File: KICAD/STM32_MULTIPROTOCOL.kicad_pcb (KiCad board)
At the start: 2 copper layers, 80 x 80 mm, 78 parts, among them T1 TestPoint, T10 TestPoint, T11 TestPoint, T12 TestPoint, T13 TestPoint, T14 TestPoint, T2 TestPoint, T3 TestPoint, T4 TestPoint, T5 TestPoint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

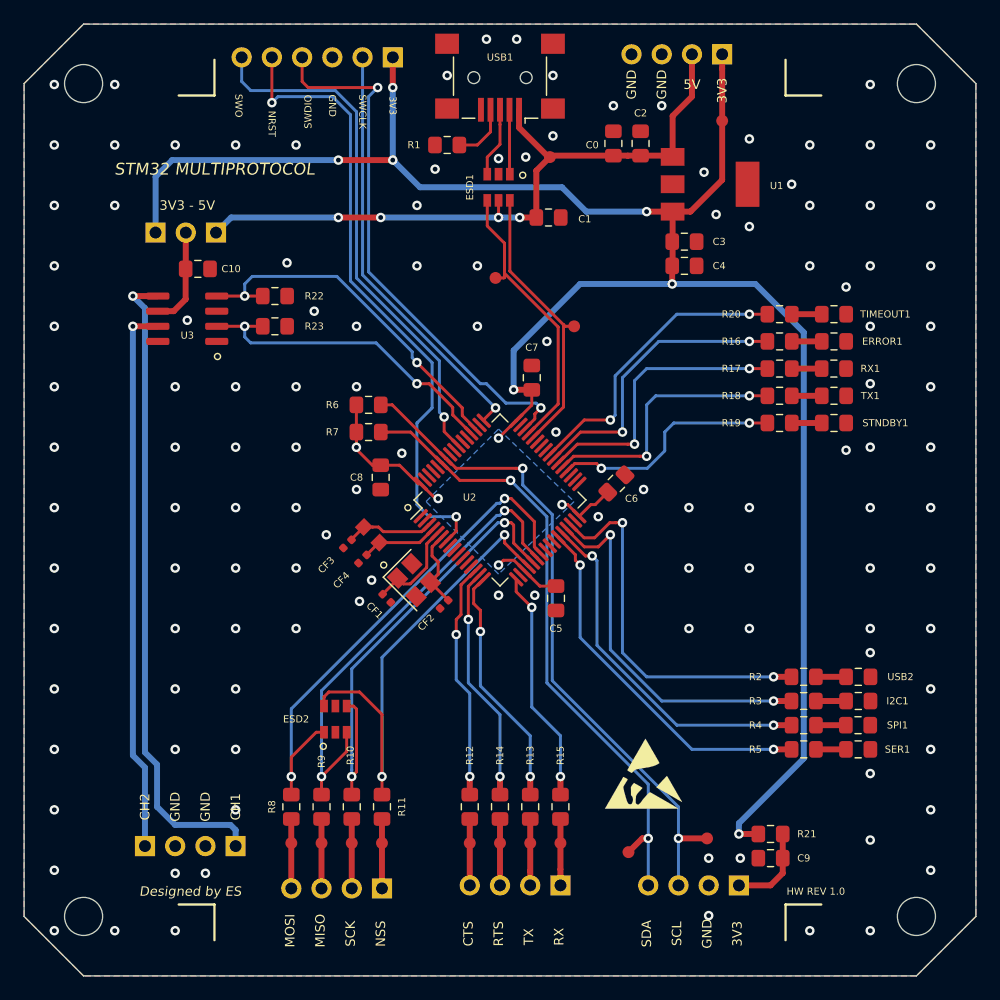
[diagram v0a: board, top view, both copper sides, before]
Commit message: uart,spi,iic pins init in input mode. USB enable fixed.
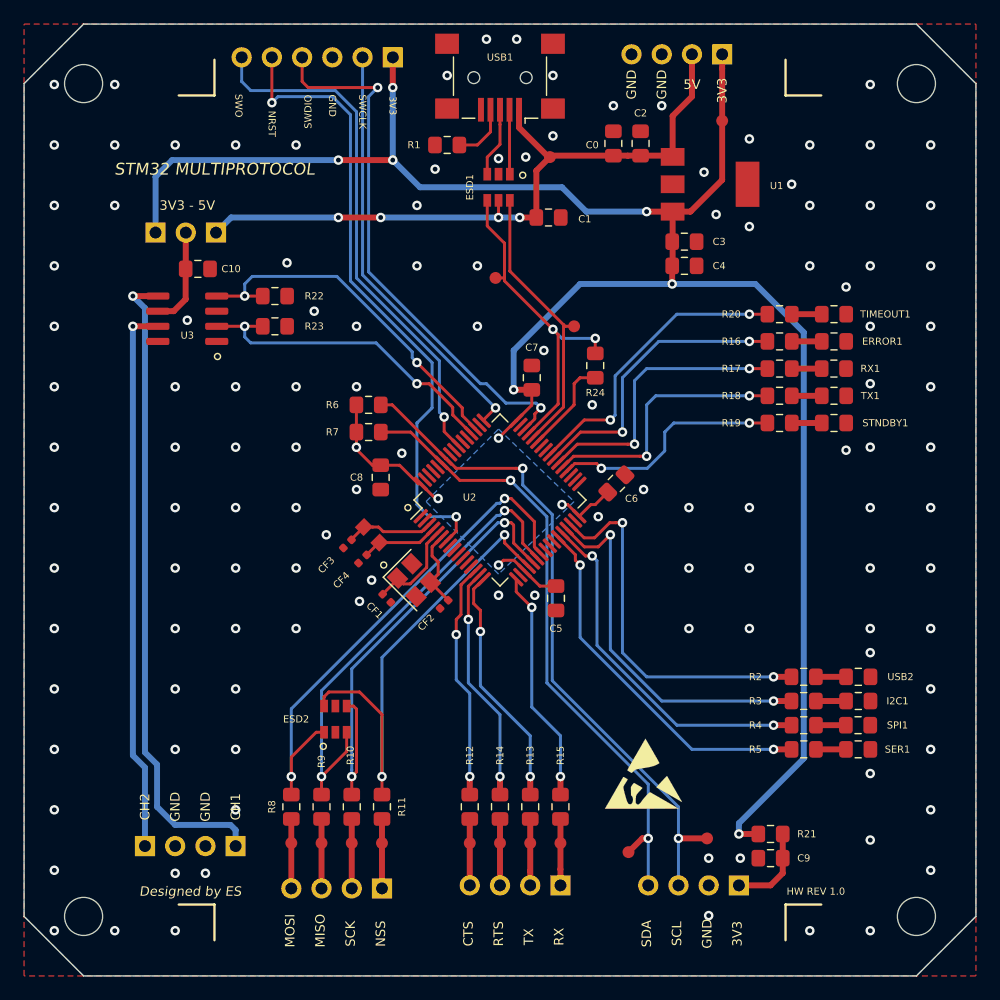
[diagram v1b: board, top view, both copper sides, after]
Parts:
- added R24: 1.5k, Resistor_SMD:R_0805_2012Metric_Pad1.15x1.40mm_HandSolder, F.Cu at (168.0, 88.7)
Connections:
- U2 pad 13: Net-(U2-Pad13) -> +3V3
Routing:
- net Net-(R24-Pad1): track 0.00 -> 8.15 mm
- net USB_DATA+: track 24.2 -> 29.0 mm, vias 0 -> 2

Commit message: added detailed BOM of the boards
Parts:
- U1: value MCP1703A-1202_SOT223 -> MIC39100-3.3WS
- renumbered Y2 to Y1, 48Mhz1 to Y2

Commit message: added pcb revision 2, fixed firmware project for cloners
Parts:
- added C11: 100nF, Resistor_SMD:R_0805_2012Metric_Pad1.15x1.40mm_HandSolder, F.Cu at (172.3, 108.8)
- added MCO1: TestPoint, TestPoint:TestPoint_Pad_D1.0mm, F.Cu at (171.3, 91.5)
- added R25: 10k, Resistor_SMD:R_0805_2012Metric_Pad1.15x1.40mm_HandSolder, F.Cu at (178.9, 99.1)
- added R26: 10k, Resistor_SMD:R_0805_2012Metric_Pad1.15x1.40mm_HandSolder, F.Cu at (178.9, 101.4)
- added TP15: TestPoint, TestPoint:TestPoint_Pad_D1.5mm, F.Cu at (177.9, 124.0)
- added U4: M24C02-WMN, Package_SO:SOIC-8_3.9x4.9mm_P1.27mm, F.Cu at (177.4, 105.7)
- T10, T11, T12, T13, T14, T5, T6, T7, T8, T9: footprint TestPoint:TestPoint_Pad_D1.0mm -> TestPoint:TestPoint_Pad_D1.5mm
- moved C9 4.78 mm to (181.2, 125.6), turned to 180 degrees
- moved R21 2.77 mm to (180.1, 128.8), turned to 90 degrees
- moved C6 2.29 mm to (169.8, 100.9), turned to 0 degrees
- moved T11 0.28 mm to (162.5, 129.6)
- moved T7 0.28 mm to (147.6, 129.6)
- moved T5 0.28 mm to (142.5, 129.6)
- moved T6 0.25 mm to (145.0, 129.6)
- moved T8 0.25 mm to (150.1, 129.6)
- moved T10 0.25 mm to (160.0, 129.6)
- moved T9 0.25 mm to (157.5, 129.6)
- moved T12 0.25 mm to (165.1, 129.6)
- turned C1 to 0 degrees
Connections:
- net I2C_SCL_PB6_PIN58 renamed I2C1_SCL_PB6_PIN58
- net I2C_SDA_PB7_PIN59 renamed I2C1_SDA_PB7_PIN59
- C1 pad 1: GND -> VUSB
- C1 pad 2: VUSB -> GND
- C9 pad 2: Net-(C9-Pad2) -> ADC12_IN15_PIN25
- I2C_OUT1 pad 1: Net-(C9-Pad2) -> Net-(I2C_OUT1-Pad1)
- R21 pad 1: Net-(C9-Pad2) -> Net-(I2C_OUT1-Pad1)
- R21 pad 2: +3V3 -> ADC12_IN15_PIN25
- U2 pad 25: Net-(U2-Pad25) -> ADC12_IN15_PIN25
- U2 pad 29: Net-(R3-Pad1) -> I2C2_SCL_PB6_PIN58
- U2 pad 30: Net-(R2-Pad1) -> I2C2_SDA_PB7_PIN59
- U2 pad 33: Net-(U2-Pad33) -> Net-(R3-Pad1)
- U2 pad 34: Net-(U2-Pad34) -> Net-(R2-Pad1)
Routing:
- net +3V3: track 188.9 -> 153.8 mm, vias 12 -> 11
- net ADC12_IN15_PIN25: track 0.00 -> 31.6 mm, vias 0 -> 2
- net I2C2_SDA_PB7_PIN59: track 0.00 -> 16.9 mm
- net I2C2_SCL_PB6_PIN58: track 0.00 -> 16.3 mm
- net Net-(MCO1-Pad1): track 0.00 -> 9.26 mm
- net Net-(C9-Pad2): track 7.40 -> 0.00 mm
- net Net-(R2-Pad1): track 31.3 -> 35.3 mm
- net Net-(R3-Pad1): track 31.4 -> 34.0 mm
- net Net-(I2C_OUT1-Pad1): track 0.00 -> 2.53 mm
- net STNDBY_LED: track 19.8 -> 20.5 mm
- net Net-(R18-Pad2): track 22.2 -> 22.8 mm
- net GND: vias 122 -> 123
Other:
- board text added: "ADC"
- board text added: "HW REV 2.0"
- board text added: "MCO"
- board text removed: "HW REV 1.0"

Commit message: updated to kicad 8
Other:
- net class Default removed
